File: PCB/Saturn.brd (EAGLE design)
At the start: 58.5 x 61 mm, 23 parts, among them U1A SN74AHCT125N, U2A SN74AHCT125N, U3A SN74AHCT125N, U4A SN74AHCT125N

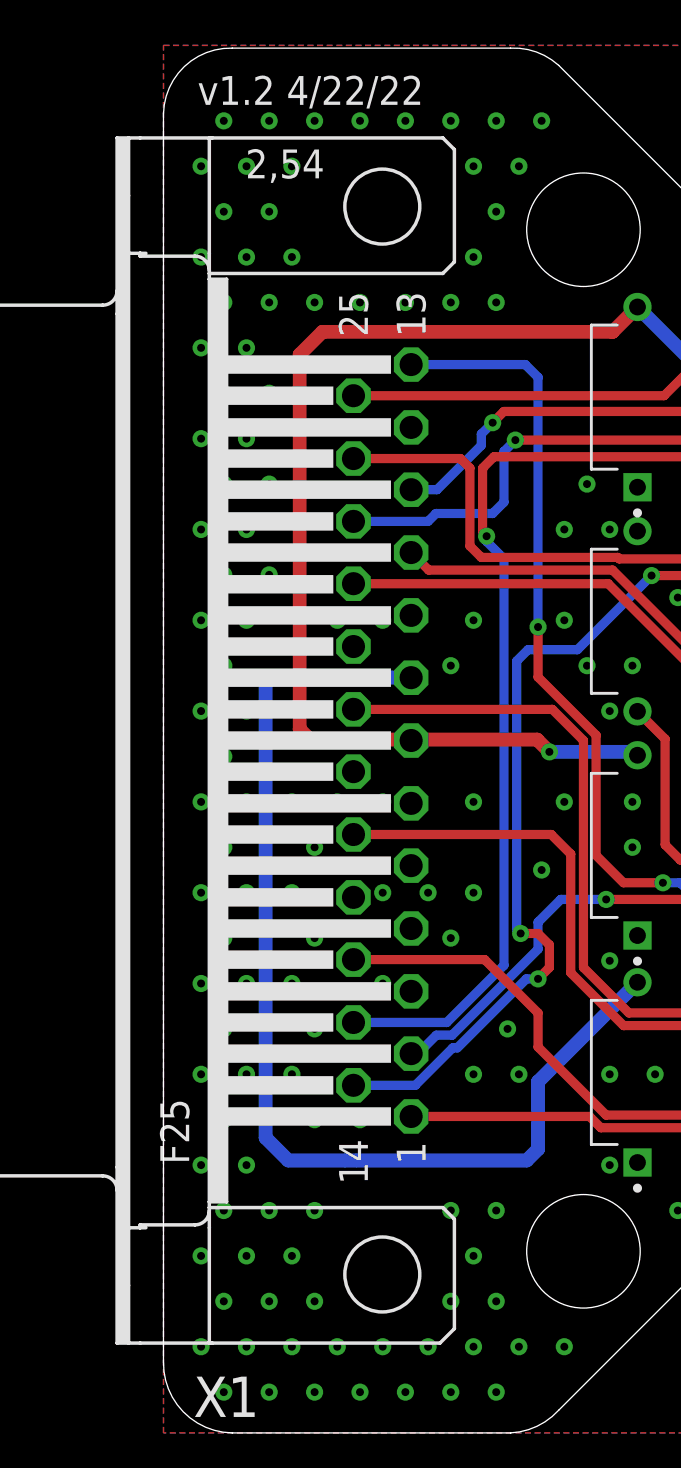
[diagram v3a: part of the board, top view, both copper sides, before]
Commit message: Added exposed GND plane at DB25 anchors
All PCBs have been update to have exposed GND plane pads for the DB25 anchor points.

This resolves Issue 54
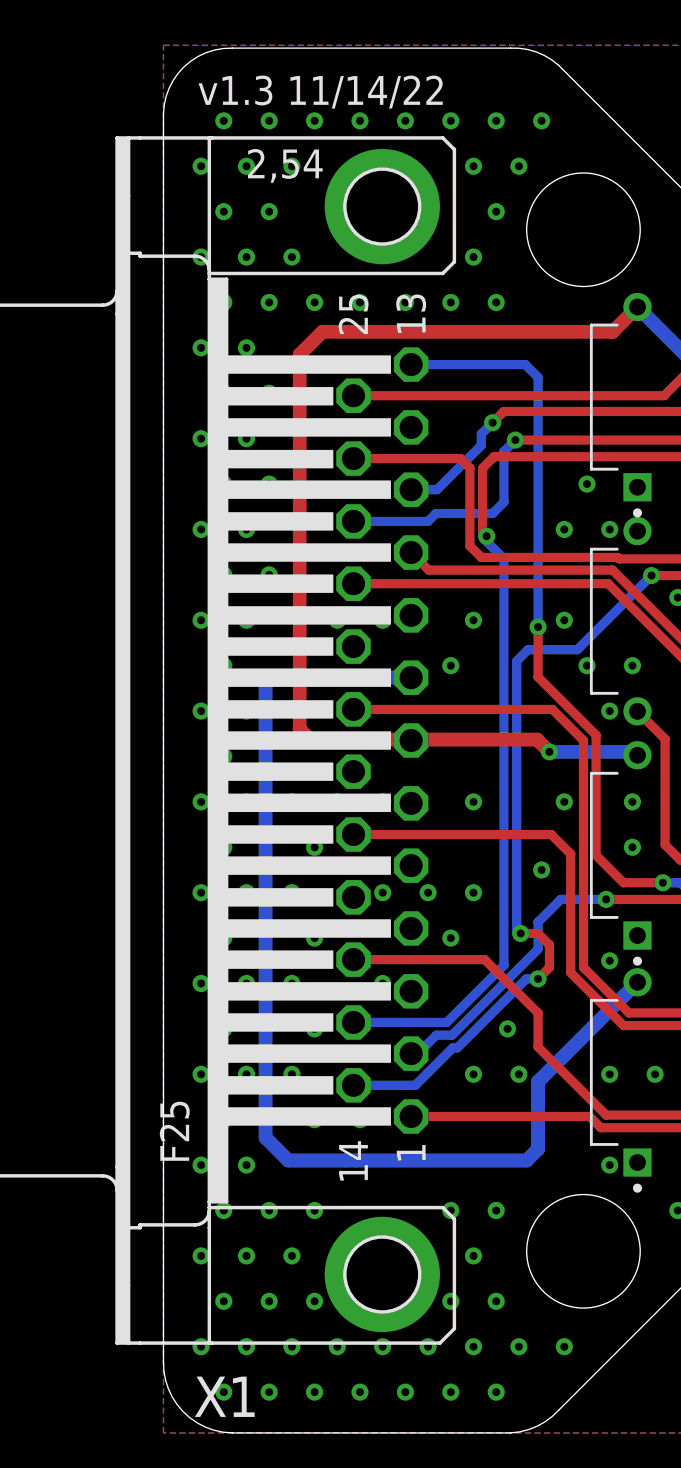
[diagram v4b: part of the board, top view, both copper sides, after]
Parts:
- X1: device SparkFun-Retired:F25H -> SparkFun-Retired:F25HP
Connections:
- net GND: now also X1.GND1, X1.GND2
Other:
- board text added: "v1.3 11/14/22"
- board text removed: "v1.2 4/22/22"
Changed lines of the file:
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@@
 <hole x="18.5" y="53" drill="5"/>
 <hole x="18.5" y="8" drill="5"/>
-<text x="1.5" y="58.5" size="1.27" layer="21">v1.2 4/22/22</text>
+<text x="1.5" y="58.5" size="1.27" layer="21">v1.3 11/14/22</text>
 <text x="49.5" y="11" size="1.778" layer="21" rot="R90">Saturn</text>
 <wire x1="58.5" y1="46.377359375" x2="58.5" y2="43.5" width="0" layer="20"/>
@@
 <attribute name="PURCHASE-URL" value="https://pricing.snapeda.com/search/part/SN74AHCT125N/?ref=eda" x="149.15" y="56.521" size="1.778" layer="27" rot="R90" display="off"/>
 </element>
-<element name="X1" library="SparkFun-Retired" package="F25H" value="" x="9.64" y="30.5" smashed="yes" rot="R90">
+<element name="X1" library="SparkFun-Retired" package="F25HP" value="" x="9.64" y="30.5" smashed="yes" rot="R90">
 <attribute name="NAME" x="4.219" y="2.48" size="1.778" layer="25" ratio="10" rot="R180"/>
 <attribute name="VALUE" x="-4.33" y="22.118" size="1.778" layer="27" ratio="10" rot="R90"/>
@@
 <via x="55.6568" y="43.7968" extent="1-16" drill="0.35"/>
 <via x="56.6568" y="45.7968" extent="1-16" drill="0.35"/>
+<contactref element="X1" pad="GND1"/>
+<contactref element="X1" pad="GND2"/>
 </signal>
 <signal name="5VIN">

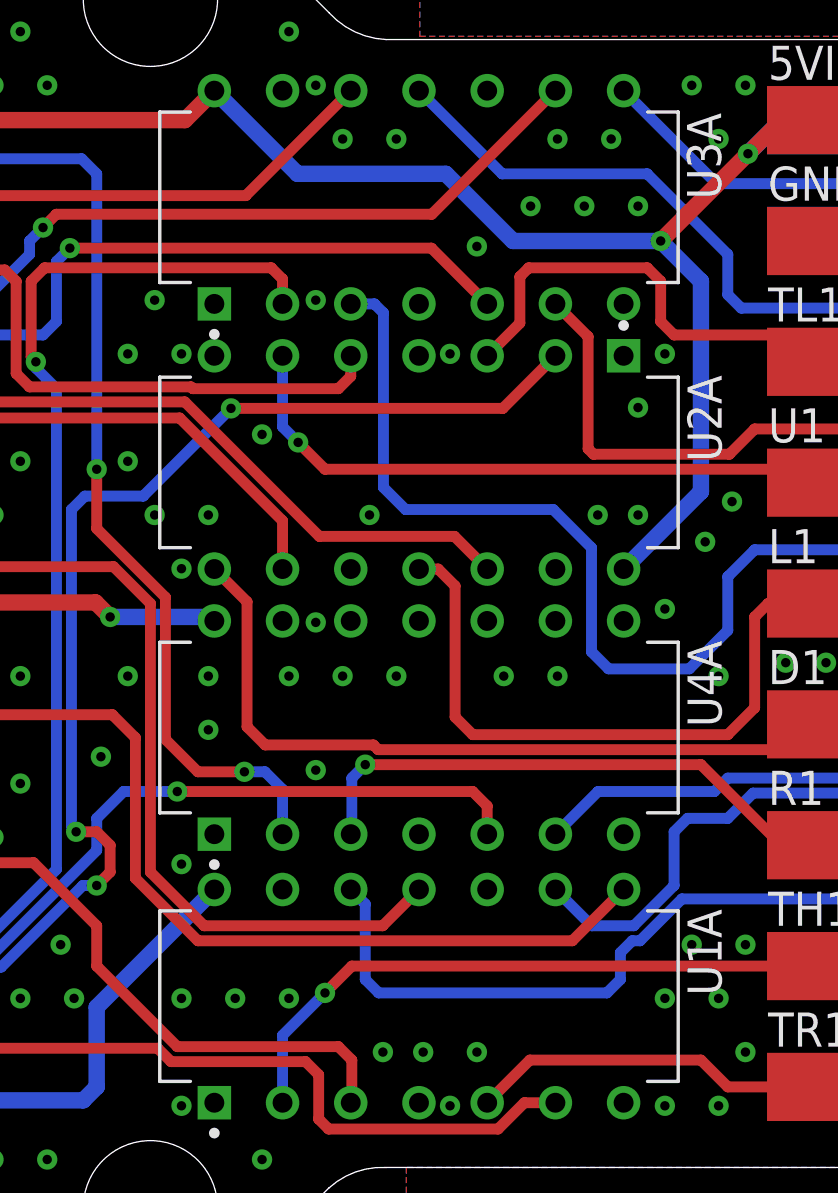
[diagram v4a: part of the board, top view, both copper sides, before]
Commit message: Silkscreen Update, Library Add, Datasheet Add
Updated the silkscreen on all PCBs that used the SN74 components as there was not orientation marker on the silkscreen.

Added Modified SN74 libraries and VB Cable Pinout image
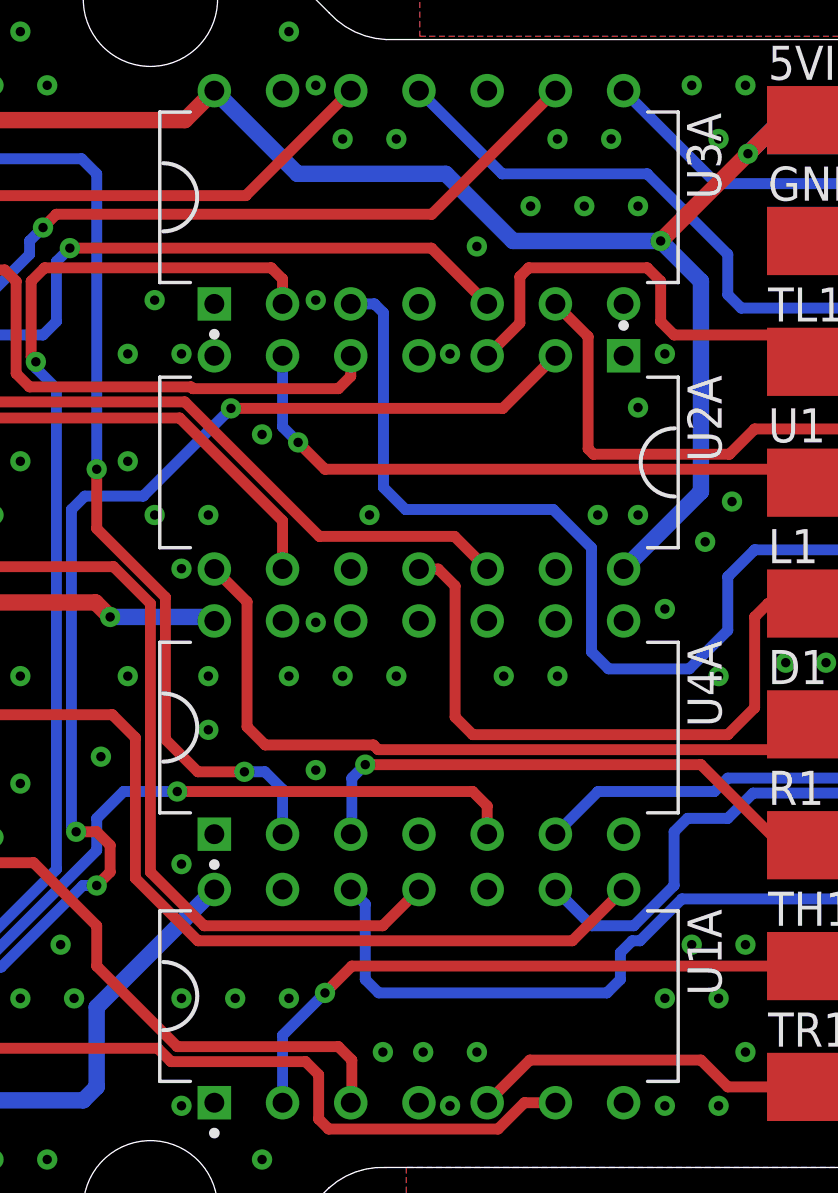
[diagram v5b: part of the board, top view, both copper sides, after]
